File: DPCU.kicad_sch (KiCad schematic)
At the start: 29 parts, among them J3 USB_C_Receptacle_USB2.0_16P, U7 STM32G474CEUx

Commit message: Add voltage divider for adj signals
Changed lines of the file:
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@@
+	(wire
+		(pts
+			(xy 81.28 160.02) (xy 95.25 160.02)
+		)
+		(stroke
+			(width 0)
+			(type default)
+		)
+	)
 	(wire
 		(pts
@@
 	(wire
 		(pts
+			(xy 81.28 157.48) (xy 95.25 157.48)
+		)
+		(stroke
+			(width 0)
+			(type default)
+		)
+	)
+	(wire
+		(pts
 			(xy 104.14 127) (xy 113.03 127)
 		)
@@
 	(wire
 		(pts
+			(xy 81.28 162.56) (xy 95.25 162.56)
+		)
+		(stroke
+			(width 0)
+			(type default)
+		)
+	)
+	(wire
+		(pts
 			(xy 161.29 88.9) (xy 175.26 88.9)
 		)
@@
 		(pts
 			(xy 245.11 34.29) (xy 255.27 34.29)
+		)
+		(stroke
+			(width 0)
+			(type default)
+		)
+	)
+	(wire
+		(pts
+			(xy 81.28 154.94) (xy 95.25 154.94)
 		)
 		(stroke
@@
 		)
 	)
+	(hierarchical_label "INT-B1"
+		(shape input)
+		(at 81.28 160.02 180)
+		(fields_autoplaced yes)
+		(effects
+			(font
+				(size 1.27 1.27)
+			)
+			(justify right)
+		)
+	)
 	(hierarchical_label "SPI1_SCK"
 		(shape output)
@@
 		)
 	)
+	(hierarchical_label "INT-A1"
+		(shape input)
+		(at 81.28 154.94 180)
+		(fields_autoplaced yes)
+		(effects
+			(font
+				(size 1.27 1.27)
+			)
+			(justify right)
+		)
+	)
 	(hierarchical_label "USART1_RX"
 		(shape input)
@@
 		)
 	)
+	(hierarchical_label "INT-B2"
+		(shape input)
+		(at 81.28 162.56 180)
+		(fields_autoplaced yes)
+		(effects
+			(font
+				(size 1.27 1.27)
+			)
+			(justify right)
+		)
+	)
 	(hierarchical_label "ACS_sides"
 		(shape input)
@@
 		(fields_autoplaced yes)
 		(effects
+			(font
+				(size 1.27 1.27)
+			)
+			(justify right)
+		)
+	)
+	(hierarchical_label "INTA-A2"
+		(shape input)
+		(at 81.28 157.48 180)
+		(fields_autoplaced yes)
+		(effects

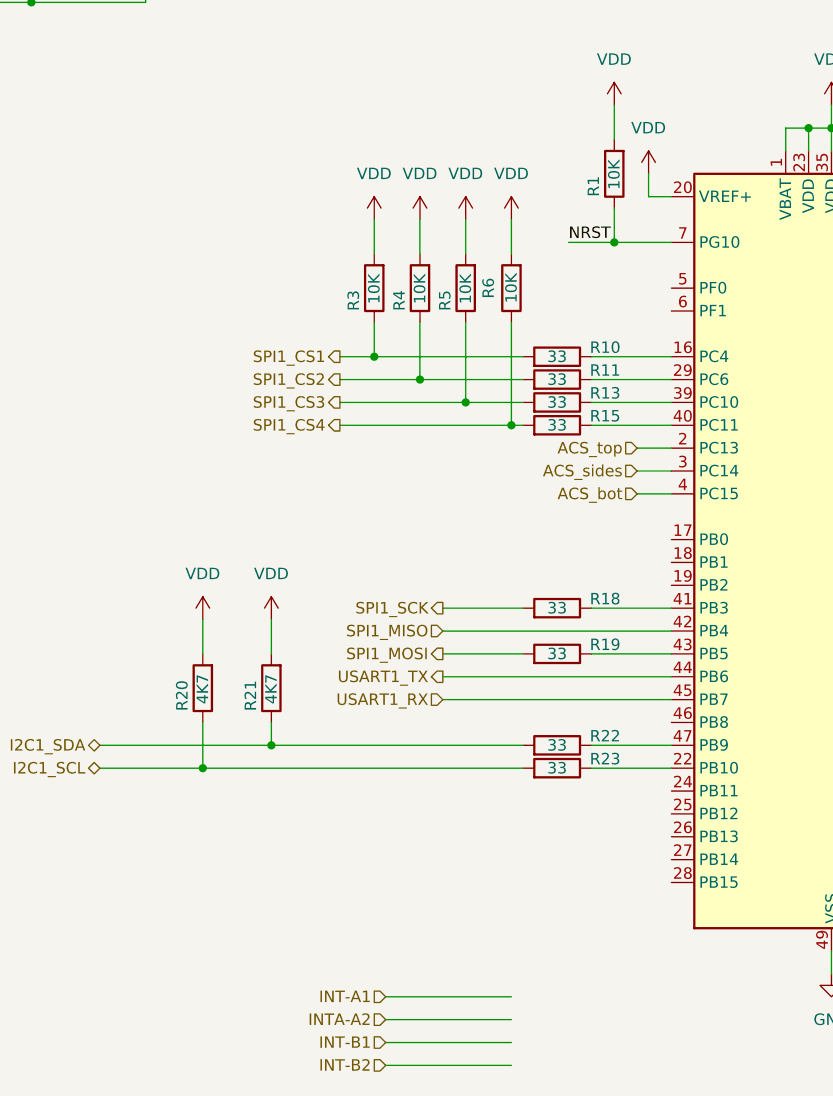
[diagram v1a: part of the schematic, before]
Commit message: data ready signals
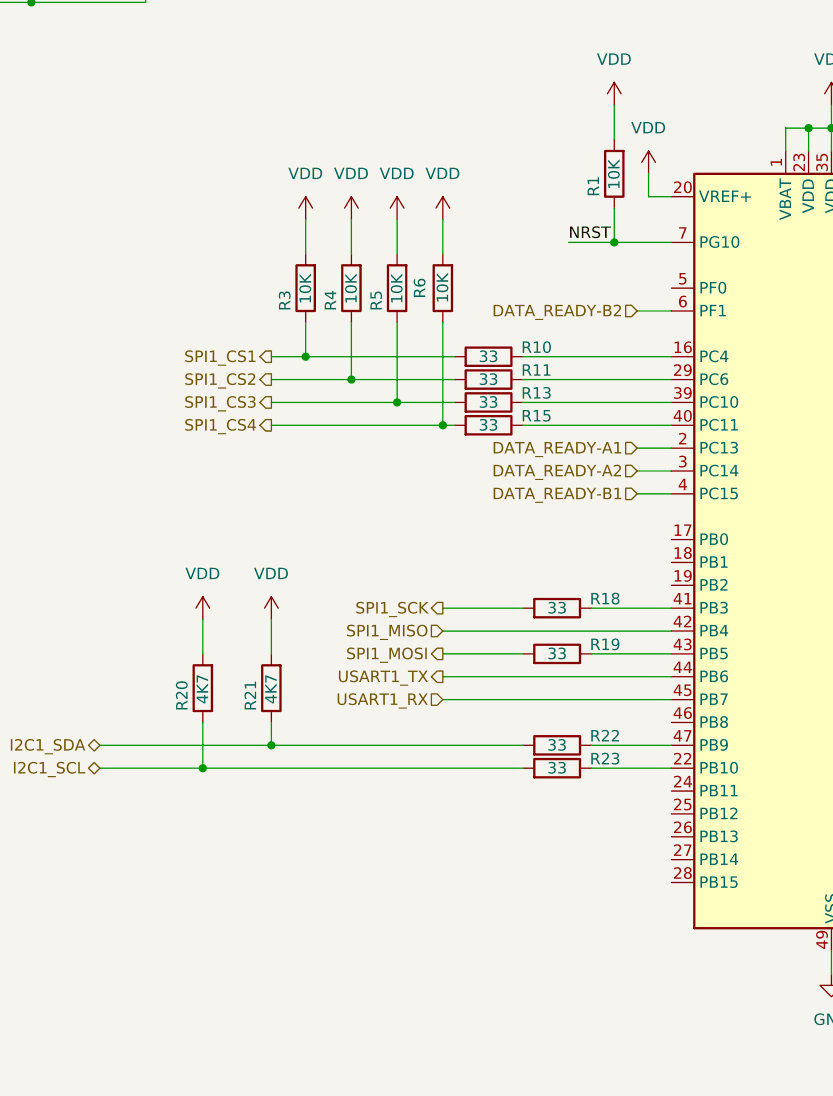
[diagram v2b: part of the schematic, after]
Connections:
- net DATA_READY-B2: now reaches U7.6 (PF1)
- net ACS_bot renamed DATA_READY-B1
- net ACS_sides renamed DATA_READY-A2
- net ACS_top renamed DATA_READY-A1
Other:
- moved on the sheet: R10, R11, R13, R15, R3, R4, R5, R6

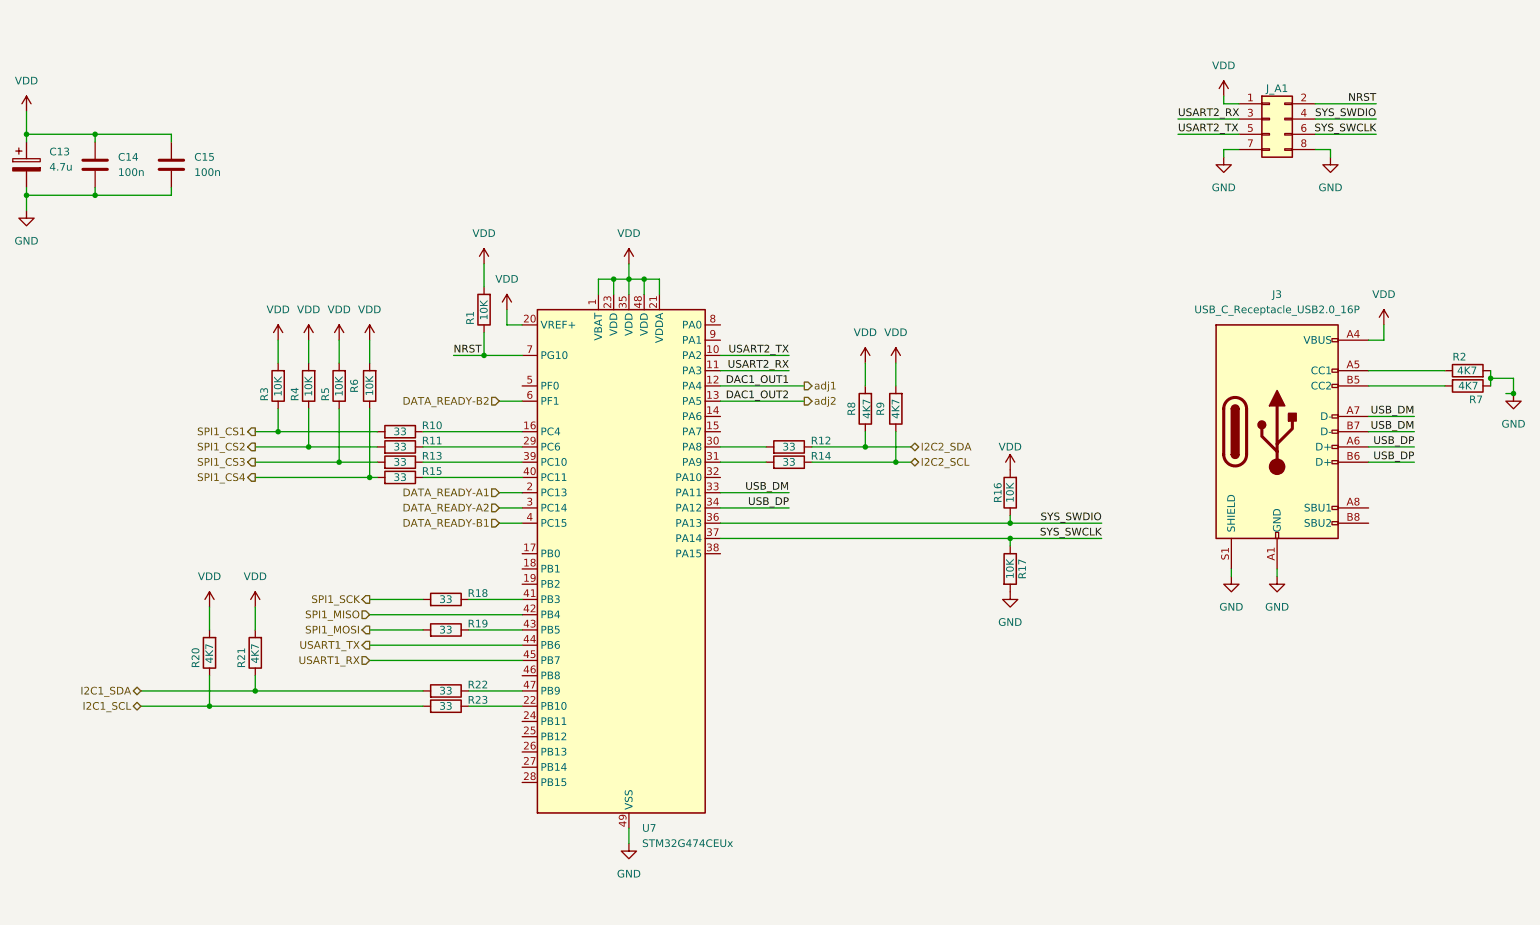
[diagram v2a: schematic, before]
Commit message: gnd and gnda
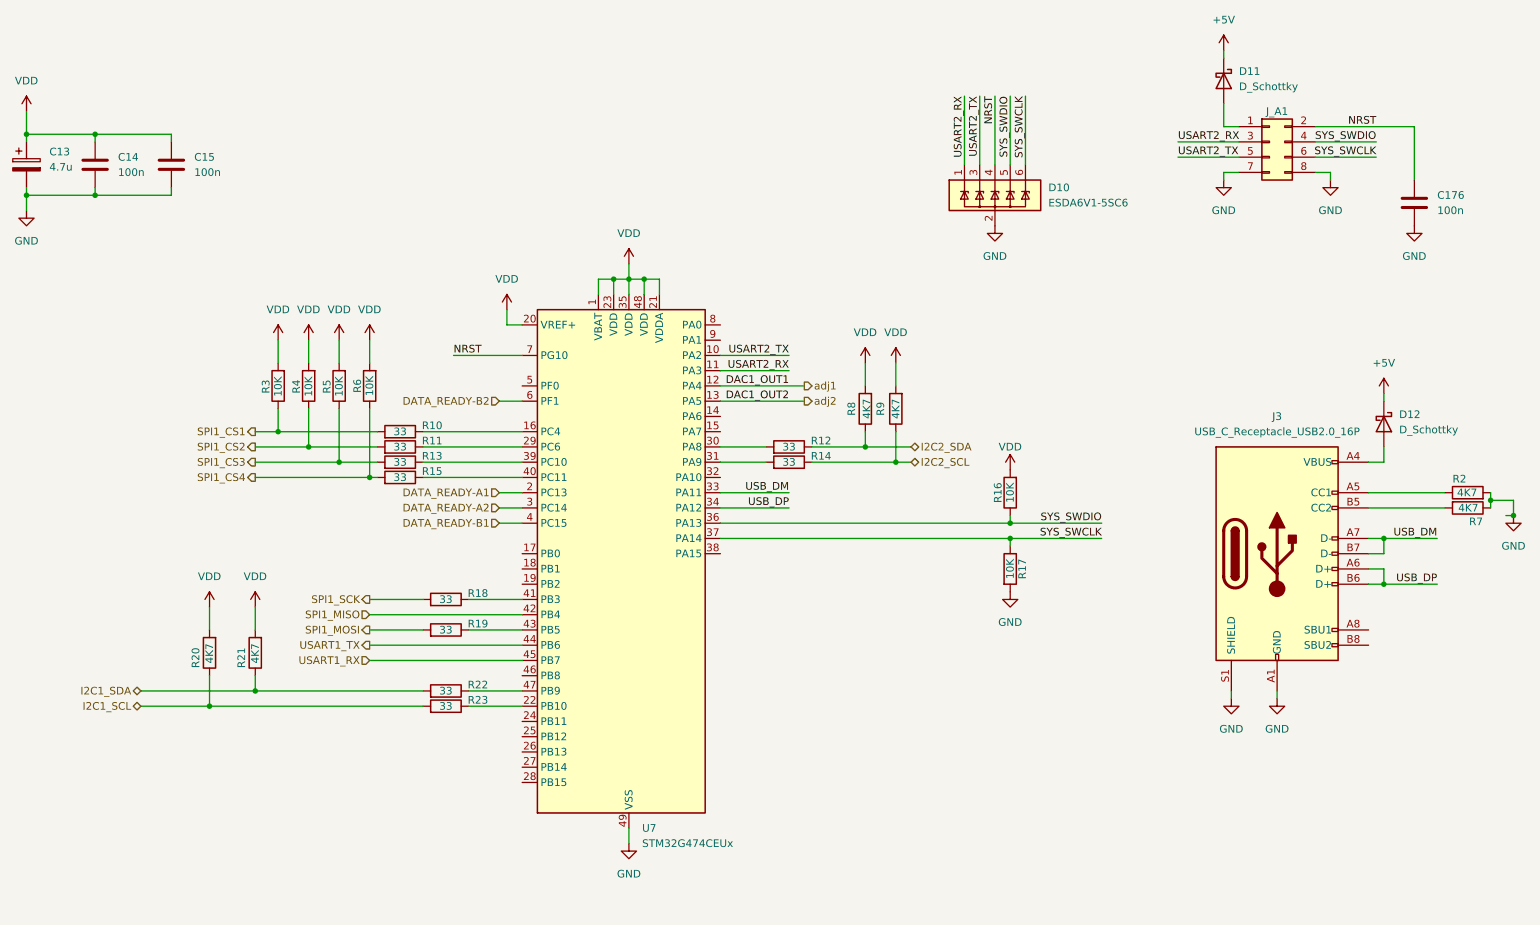
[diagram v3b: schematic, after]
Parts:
- removed R1: 10K, Resistor_SMD:R_0603_1608Metric_Pad0.98x0.95mm_HandSolder, symbol Device:R
- added C176: 100n, symbol Device:C
- added D10: ESDA6V1-5SC6, Package_TO_SOT_SMD:SOT-23-6, symbol Power_Protection:ESDA6V1-5SC6
- added D11, D12: D_Schottky, symbol Device:D_Schottky
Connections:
- net GND: now also C176.2, D10.2 (GND)
- net NRST: now also C176.1, D10.4 (IO3)
- net SYS_SWCLK: now also D10.6 (IO5)
- net SYS_SWDIO: now also D10.5 (IO4)
- net USART2_RX: now also D10.1 (IO1)
- net USART2_TX: now also D10.3 (IO2)
- net VDD: no longer J3.A4 (VBUS), J3.A9 (VBUS), J3.B4 (VBUS), J3.B9 (VBUS), J_A1.1 (Pin_1)
- new net: D12.2 (A), J3.A4 (VBUS), J3.A9 (VBUS), J3.B4 (VBUS), J3.B9 (VBUS)
- new net: D11.2 (A), J_A1.1 (Pin_1)
- new net +5V: D11.1 (K), D12.1 (K)
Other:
- moved on the sheet: J3, J_A1, R2, R7
